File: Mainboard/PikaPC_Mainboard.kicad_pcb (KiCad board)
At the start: 2 copper layers, 190.5 x 147.3 mm, 88 parts, among them J1 Conn_02x08_Odd_Even, J10 Conn_01x08, J11 Conn_01x08, J12 Conn_01x08, J13 Conn_01x08, J14 Conn_01x08, J15 Conn_01x08, J16 Conn_01x08, J17 Conn_01x08, J18 Conn_01x10, J19 Conn_02x05_Odd_Even, J5 DIN41612_03x32_C_Split, J6 Mini-DIN-6, J7 Mini-DIN-6, J8 Conn_01x06, J9 Conn_01x08, SW1 SW_Push_DPDT, SW2 SW_Push, U1 PPC403GA, U10 74LS07, U11 86C325, U12 GD75232N, U13 74LVC125, U14 MCP120-315GI/TO, U15 AS6C4008-55PCN, U16 AS6C4008-55PCN, U17 ATF1504, U18 T224162B, U19 T224162B, U2 SN74LVC245A, U20 T224162B, U21 T224162B, U22 74LVC125, U3 SST39VF010, U4 SN74LVC245A, U5 SN74LVC245A, U6 SN74LVC245A, U7 8042 PS/2, U8 ATF22V10C, U9 74LS04, Y1 25M, Y2 7M3728, Y3 14M31818

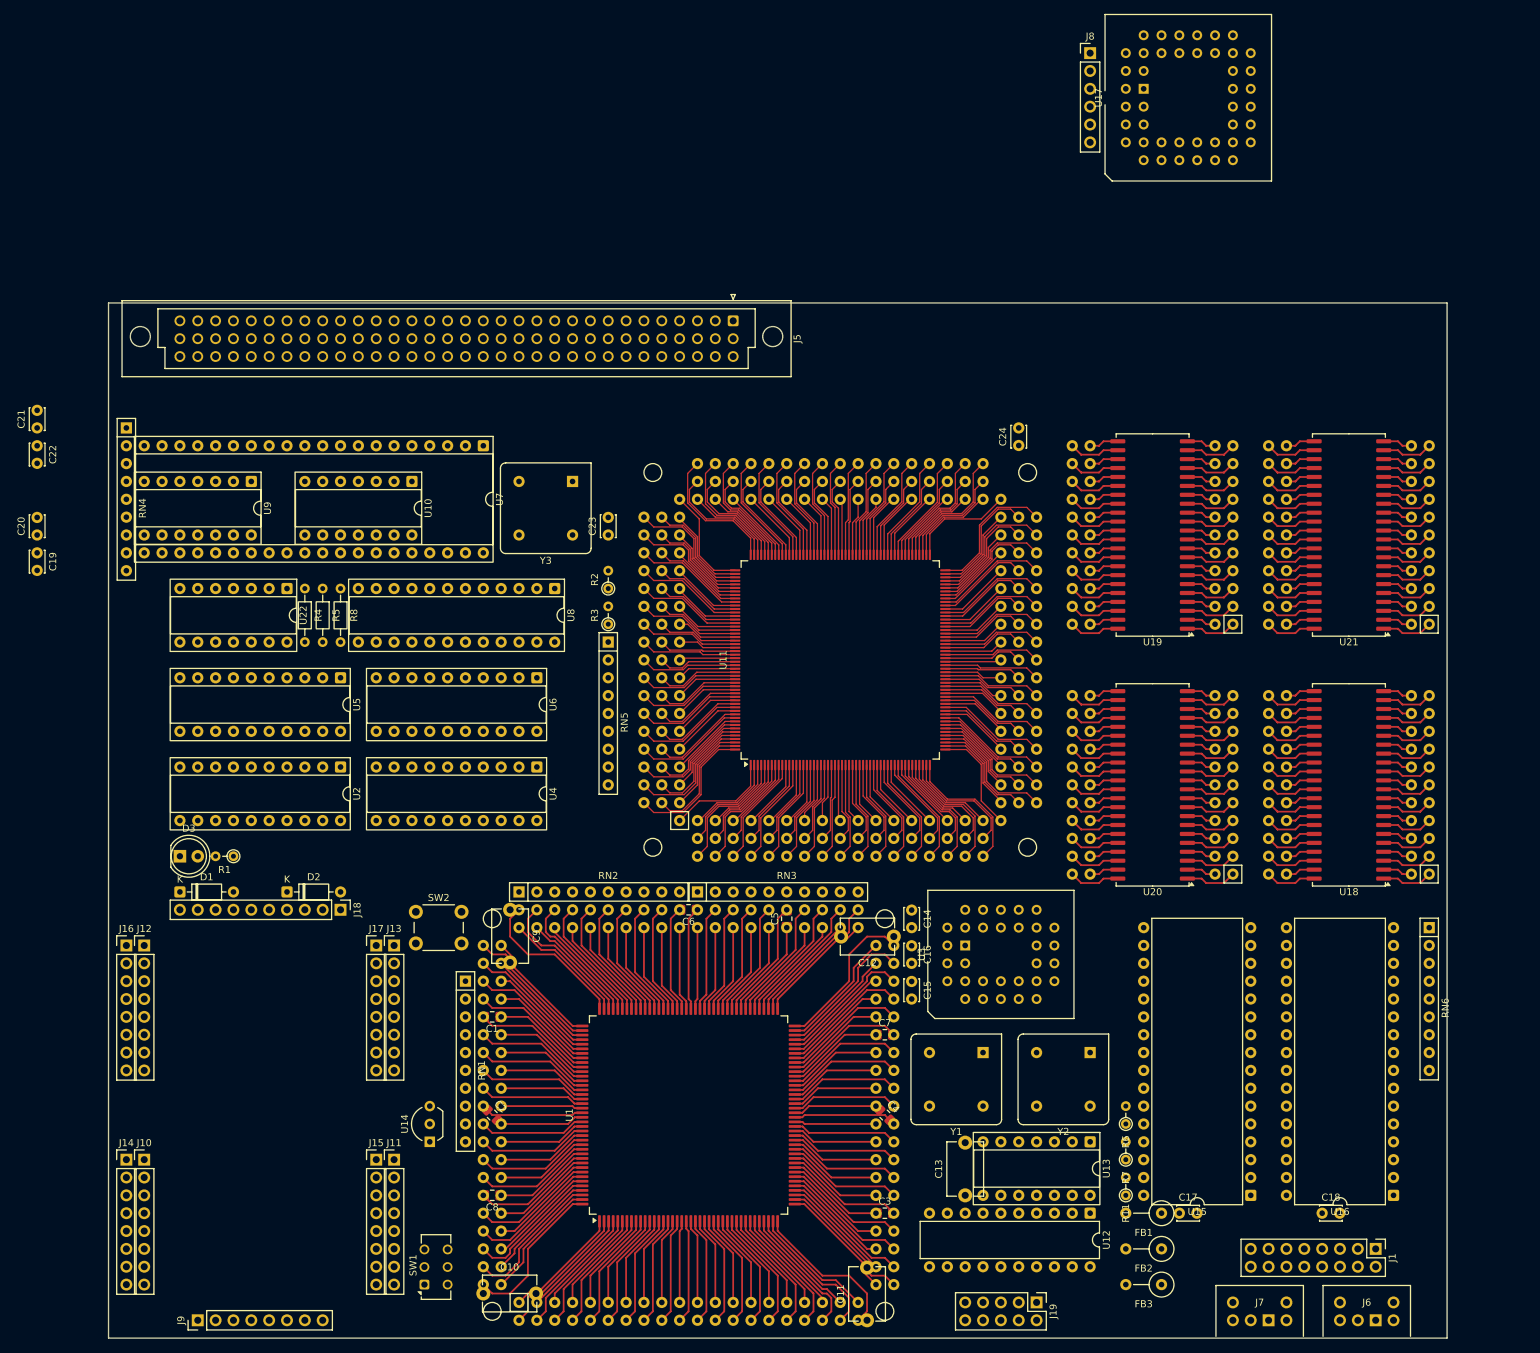
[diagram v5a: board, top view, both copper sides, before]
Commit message: New peripheral bus
- additional bus transceivers for byte lane steering to VLB
- replace 22V10 with 1504 for peripheral bus control logic
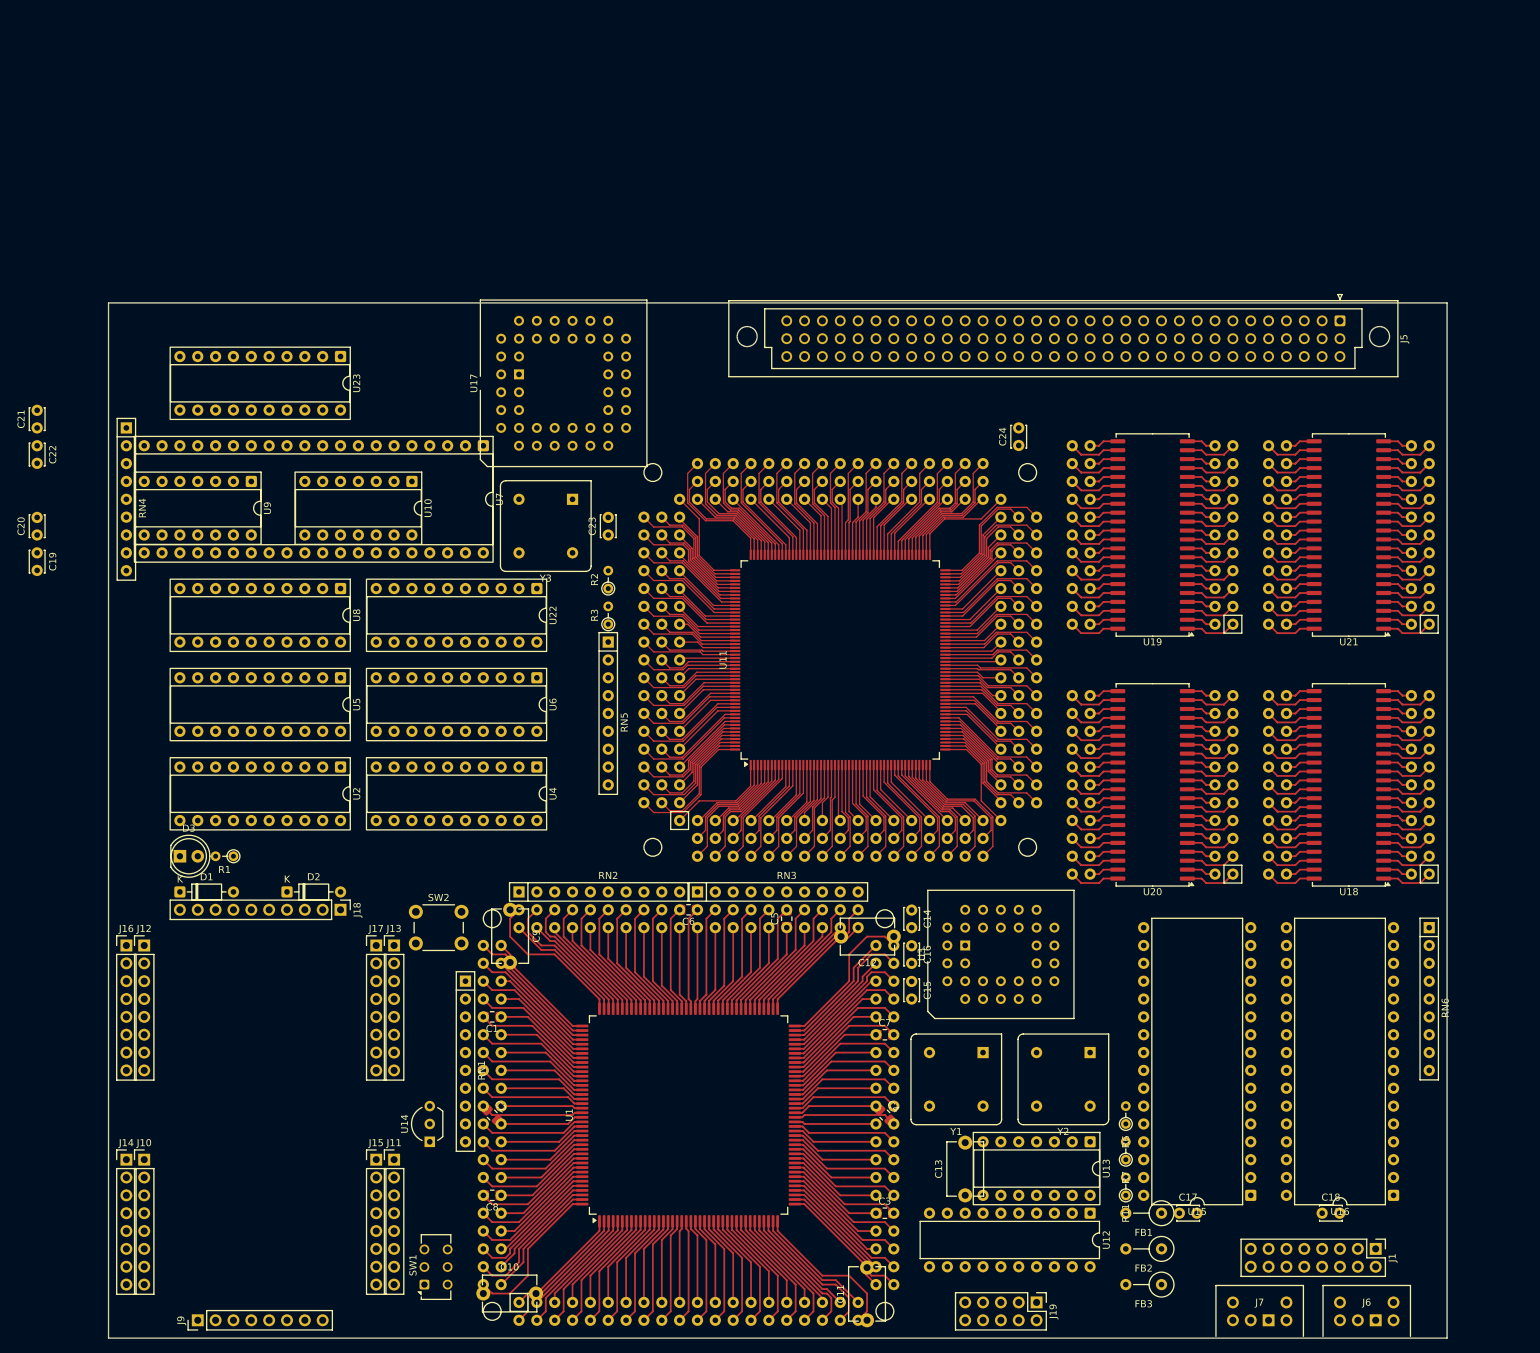
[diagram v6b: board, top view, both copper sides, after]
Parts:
- removed J8: Conn_01x06, Connector_PinHeader_2.54mm:PinHeader_1x06_P2.54mm_Vertical
- removed R4, R5, R8: 1k, Resistor_THT:R_Axial_DIN0204_L3.6mm_D1.6mm_P7.62mm_Horizontal
- added U23: SN74LVC245A, Package_DIP:DIP-20_W7.62mm_Socket, F.Cu at (104.1, 20.3)
- U22: value 74LVC125 -> SN74LVC245A; footprint Package_DIP:DIP-14_W7.62mm_Socket -> Package_DIP:DIP-20_W7.62mm_Socket
- U8: value ATF22V10C -> SN74LVC245A; footprint Package_DIP:DIP-24_W7.62mm_Socket -> Package_DIP:DIP-20_W7.62mm_Socket
- moved U17 97.7 mm to (129.5, 22.9)
- moved J5 86.4 mm to (246.4, 15.2)
- moved U22 35.6 mm to (132.1, 53.3)
- moved U8 30.5 mm to (104.1, 53.3)
- moved Y3 2.54 mm to (137.2, 40.6)
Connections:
- net /PD0 renamed /VD24
- net /PD1 renamed /VD25
- net /PD2 renamed /VD26
- net /PD3 renamed /VD27
- net /PD4 renamed /VD28
- net /PD5 renamed /VD29
- net /PD6 renamed /VD30
- net /PD7 renamed /VD31
- RN4 pad 8: /~{VID-SRDYn} -> /~{VID-SRDY}
- U11 pad 10: /PD15 -> /VD23
- U11 pad 11: /PD14 -> /VD22
- U11 pad 13: /PD13 -> /VD21
- U11 pad 14: /PD12 -> /VD20
- U11 pad 15: /PD11 -> /VD19
- U11 pad 16: /PD10 -> /VD18
- U11 pad 17: /PD9 -> /VD17
- U11 pad 18: /PD8 -> /VD16
- U11 pad 194: /~{SysClk-5v} -> /SysClk-5v
- U11 pad 23: /~{VID-SRDYn} -> /~{VID-SRDY}
- U11 pad 28: /PD23 -> /VD15
- U11 pad 29: /PD22 -> /VD14
- U11 pad 30: /PD21 -> /VD13
- U11 pad 31: /PD20 -> /VD12
- U11 pad 33: /PD19 -> /VD11
- U11 pad 34: /PD18 -> /VD10
- U11 pad 35: /PD17 -> /VD9
- U11 pad 36: /PD16 -> /VD8
- U11 pad 39: /PD31 -> /VD7
- U11 pad 40: /PD30 -> /VD6
- U11 pad 41: /PD29 -> /VD5
- U11 pad 42: /PD28 -> /VD4
- U11 pad 43: /PD27 -> /VD3
- U11 pad 44: /PD26 -> /VD2
- U11 pad 45: /PD25 -> /VD1
- U11 pad 46: /PD24 -> /VD0
- U11 pad 8: /A23 -> /VID-M/~{IO}
- U13 pad 1: /~{VID-SRDYn} -> /~{VID-SRDY}
- U13 pad 4: /~{SDReady} -> unconnected-(U13-Pad4)
- U13 pad 5: +3.3V -> unconnected-(U13-Pad5)
- U13 pad 6: /Ready -> unconnected-(U13-Pad6)
- U17 pad 11: /R/~{W} -> /~{PB32}
- U17 pad 12: /~{SDReady} -> /~{VID-RDYIN}
- U17 pad 13: unconnected-(U17-TMS/IO32-Pad13) -> /PB-TMS
- U17 pad 14: unconnected-(U17-IO30-Pad14) -> /~{VID-SBE1}
- U17 pad 16: unconnected-(U17-IO25-Pad16) -> /~{VID-SBE3}
- U17 pad 17: /INT1 -> /~{VID-SBE0}
- U17 pad 18: /PD31 -> /~{VID-SBE2}
- U17 pad 19: /PD30 -> /VID-SAUP1
- U17 pad 20: /PD29 -> /VID-SAUP2
- U17 pad 21: /PD28 -> /VID-M/~{IO}
- U17 pad 25: unconnected-(U17-IO35-Pad25) -> /~{VID-SRDY}
- U17 pad 26: unconnected-(U17-IO36-Pad26) -> /A23
- U17 pad 27: unconnected-(U17-IO37-Pad27) -> /~{WBE2}
- U17 pad 28: unconnected-(U17-IO40-Pad28) -> /A1/~{WBE1}
- U17 pad 29: unconnected-(U17-IO41-Pad29) -> /~{WBE3}
- U17 pad 31: unconnected-(U17-IO46-Pad31) -> /A0/~{WBE0}
- U17 pad 32: unconnected-(U17-TCK/IO48-Pad32) -> /PB-TCK
- U17 pad 33: unconnected-(U17-IO49-Pad33) -> /~{OE}
- U17 pad 34: unconnected-(U17-IO51-Pad34) -> /~{CS6}
- U17 pad 36: unconnected-(U17-IO52-Pad36) -> /~{CS4}
- U17 pad 37: /SDCS -> /~{CS5}
- U17 pad 38: unconnected-(U17-TDO/IO56-Pad38) -> /PB-TDO
- U17 pad 39: /SDSCK -> /~{CS7}
- U17 pad 4: /PD27 -> /~{VID-ADS}
- U17 pad 40: /SDMOSI -> /~{CS2}
- U17 pad 41: /SDMISO -> /~{CS3}
- U17 pad 5: /PD26 -> /~{PBE0}
- U17 pad 6: /PD25 -> /~{PBE1}
- U17 pad 7: unconnected-(U17-TDI/IO8-Pad7) -> /PB-TDI
- U17 pad 8: /PD24 -> /~{PBE3}
- U17 pad 9: /~{CS4} -> /~{PBE2}
- U2 pad 19: /~{PDBEN} -> /~{PB32}
- U2 pad 2: /PD16 -> /VD8
- U2 pad 3: /PD17 -> /VD9
- U2 pad 4: /PD18 -> /VD10
- U2 pad 5: /PD19 -> /VD11
- U2 pad 6: /PD20 -> /VD12
- U2 pad 7: /PD21 -> /VD13
- U2 pad 8: /PD22 -> /VD14
- U2 pad 9: /PD23 -> /VD15
- U22 pad 1: /~{CS2} -> /R/~{W}
- U22 pad 10: /~{CS3} -> GND
- U22 pad 11: /VID-SAUP2 -> /D31
- U22 pad 12: /A25 -> /D30
- U22 pad 13: /~{VID-SAU-E} -> /D29
- U22 pad 14: +3.3V -> /D28
- U22 pad 2: GND -> /VD16
- U22 pad 3: /~{VID-SAU-E} -> /VD17
- U22 pad 4: /~{VID-SAU-E} -> /VD18
- U22 pad 5: /A24 -> /VD19
- U22 pad 6: /VID-SAUP1 -> /VD20
- U22 pad 7: GND -> /VD21
- U22 pad 8: /~{VID-SAU-E} -> /VD22
- U22 pad 9: GND -> /VD23
- U4 pad 19: /~{PDBEN} -> /~{PBE0}
- U4 pad 2: /PD24 -> /VD0
- U4 pad 3: /PD25 -> /VD1
- U4 pad 4: /PD26 -> /VD2
- U4 pad 5: /PD27 -> /VD3
- U4 pad 6: /PD28 -> /VD4
- U4 pad 7: /PD29 -> /VD5
- U4 pad 8: /PD30 -> /VD6
- U4 pad 9: /PD31 -> /VD7
- U5 pad 19: /~{PDBEN} -> /~{PB32}
- U6 pad 19: /~{PDBEN} -> /~{PB32}
- U6 pad 2: /PD8 -> /VD16
- U6 pad 3: /PD9 -> /VD17
- U6 pad 4: /PD10 -> /VD18
- U6 pad 5: /PD11 -> /VD19
- U6 pad 6: /PD12 -> /VD20
- U6 pad 7: /PD13 -> /VD21
- U6 pad 8: /PD14 -> /VD22
- U6 pad 9: /PD15 -> /VD23
- U7 pad 12: /PD24 -> /VD0
- U7 pad 13: /PD25 -> /VD1
- U7 pad 14: /PD26 -> /VD2
- U7 pad 15: /PD27 -> /VD3
- U7 pad 16: /PD28 -> /VD4
- U7 pad 17: /PD29 -> /VD5
- U7 pad 18: /PD30 -> /VD6
- U7 pad 19: /PD31 -> /VD7
- U8 pad 1: /SysClk-5v -> /R/~{W}
- U8 pad 10: /~{WBE3} -> GND
- U8 pad 11: /~{VID-SRDYn} -> /D31
- U8 pad 12: GND -> /D30
- U8 pad 13: unconnected-(U8-I13-Pad13) -> /D29
- U8 pad 14: unconnected-(U8-IO14-Pad14) -> /D28
- U8 pad 15: unconnected-(U8-IO15-Pad15) -> /D27
- U8 pad 16: /~{VID-ADS} -> /D26
- U8 pad 17: /~{VID-SBE0} -> /D25
- U8 pad 18: /~{VID-SBE1} -> /D24
- U8 pad 19: /~{VID-SBE2} -> /~{PBE1}
- U8 pad 2: /~{CS2} -> /VD8
- U8 pad 20: /~{VID-SBE3} -> +3.3V
- U8 pad 3: /~{CS3} -> /VD9
- U8 pad 4: /~{CS4} -> /VD10
- U8 pad 5: /~{CS5} -> /VD11
- U8 pad 6: /~{OE} -> /VD12
- U8 pad 7: /A0/~{WBE0} -> /VD13
- U8 pad 8: /A1/~{WBE1} -> /VD14
- U8 pad 9: /~{WBE2} -> /VD15
- U9 pad 12: /~{SysClk-5v} -> unconnected-(U9-Pad12)
- U9 pad 13: /SysClk-5v -> unconnected-(U9-Pad13)
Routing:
- net /VD0: track 0.00 -> 17.1 mm
- net /PD24: track 17.1 -> 0.00 mm
- net /VD3: track 0.00 -> 16.0 mm
- net /PD27: track 16.0 -> 0.00 mm
- net /VD23: track 0.00 -> 15.9 mm
- net /PD15: track 15.9 -> 0.00 mm
- net /VD6: track 0.00 -> 15.5 mm
- net /PD30: track 15.5 -> 0.00 mm
- net /VD21: track 0.00 -> 15.4 mm
- net /PD13: track 15.4 -> 0.00 mm
- net /VD18: track 0.00 -> 15.0 mm
- net /PD10: track 15.0 -> 0.00 mm
- net /VD10: track 0.00 -> 14.7 mm
- net /PD18: track 14.7 -> 0.00 mm
- net /VD1: track 0.00 -> 14.5 mm
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
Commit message: New peripheral bus debugging
- add pull-ups to bus transceiver enable signals for debugging
- change reset pull-up to 1k to help with rise times
- update bank registers configuration for new peripheral bus
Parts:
- added RN7: 9A103J, Resistor_THT:R_Array_SIP9, F.Cu at (73.7, 55.9)
- RN3: value 10X-1-472LF -> 10X-1-102LF

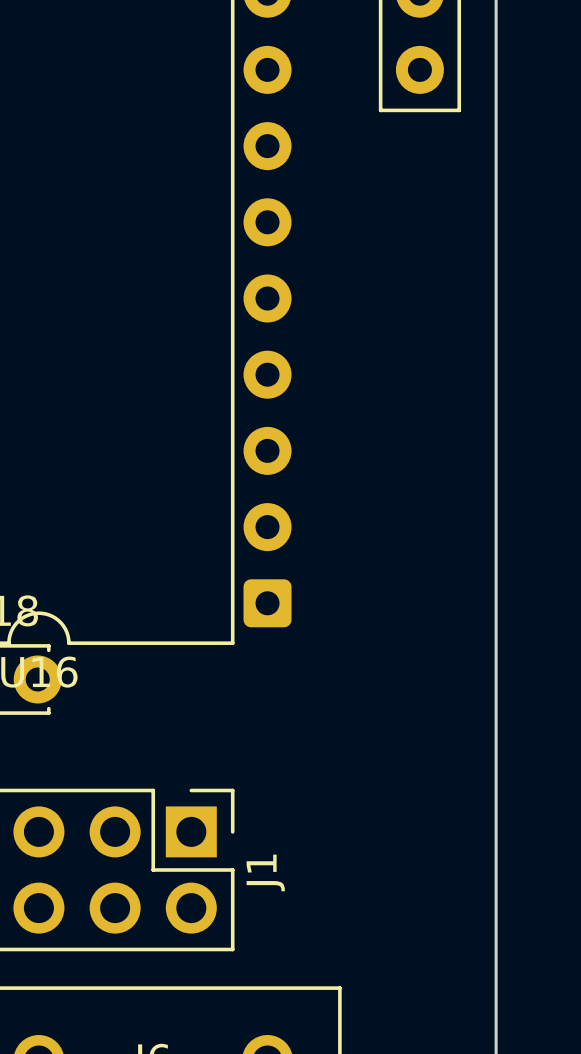
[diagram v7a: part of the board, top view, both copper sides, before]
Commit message: VRAM control debugging
- add strapping resistors for slow vram cycles
- fix swapped CAS2 & CAS3 pins on ViRGE symbol
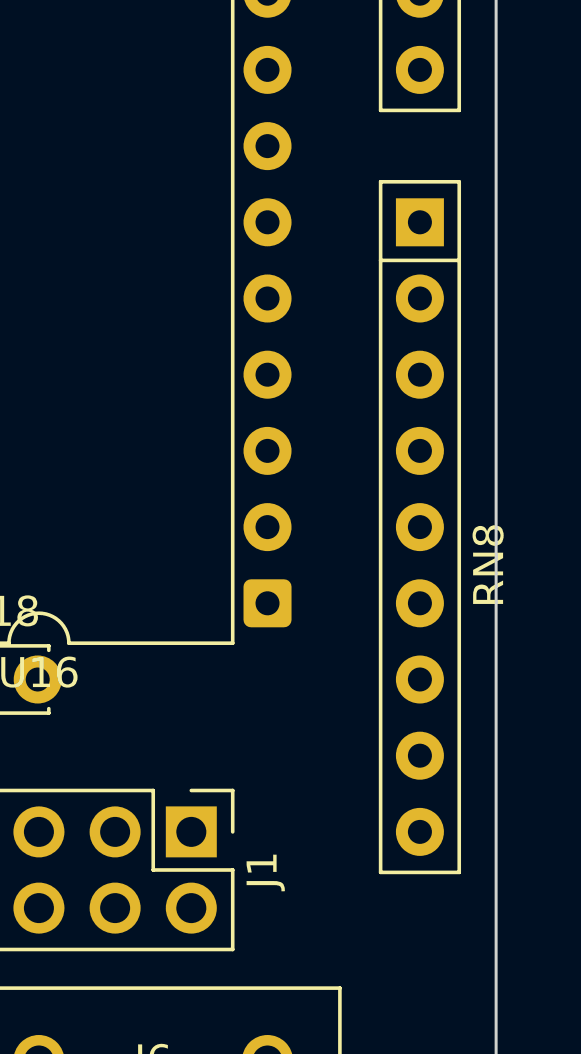
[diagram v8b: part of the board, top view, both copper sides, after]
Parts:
- added RN8: 9A103J, Resistor_THT:R_Array_SIP9, F.Cu at (259.1, 127.0)
- RN7: value 9A103J -> 10X-1-472F
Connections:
- U11 pad 82: /~{VMCAS2} -> /~{VMCAS3}
- U11 pad 83: /~{VMCAS3} -> /~{VMCAS2}
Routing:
- net /~{VMCAS3}: track 18.5 -> 15.9 mm
- net /~{VMCAS2}: track 19.0 -> 21.5 mm
